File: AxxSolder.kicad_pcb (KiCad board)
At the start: 2 copper layers, 39 x 71 mm, 91 parts, among them IC1 LTC4440AHMS8E-5#PBF, IC2 STM32G431KBT6, IC3 TMP236AQDBZRQ1, IC4 OPA2333AIDRBR, IC5 STM32G431KBT6, IC6 TPS54302DDCR, J1 Conn_01x07_Male, J4 Conn_01x07_Male, Q2 2N7002NXAKR, U1 PEC11L-4220F-S0015, U2 BSC014N04LS

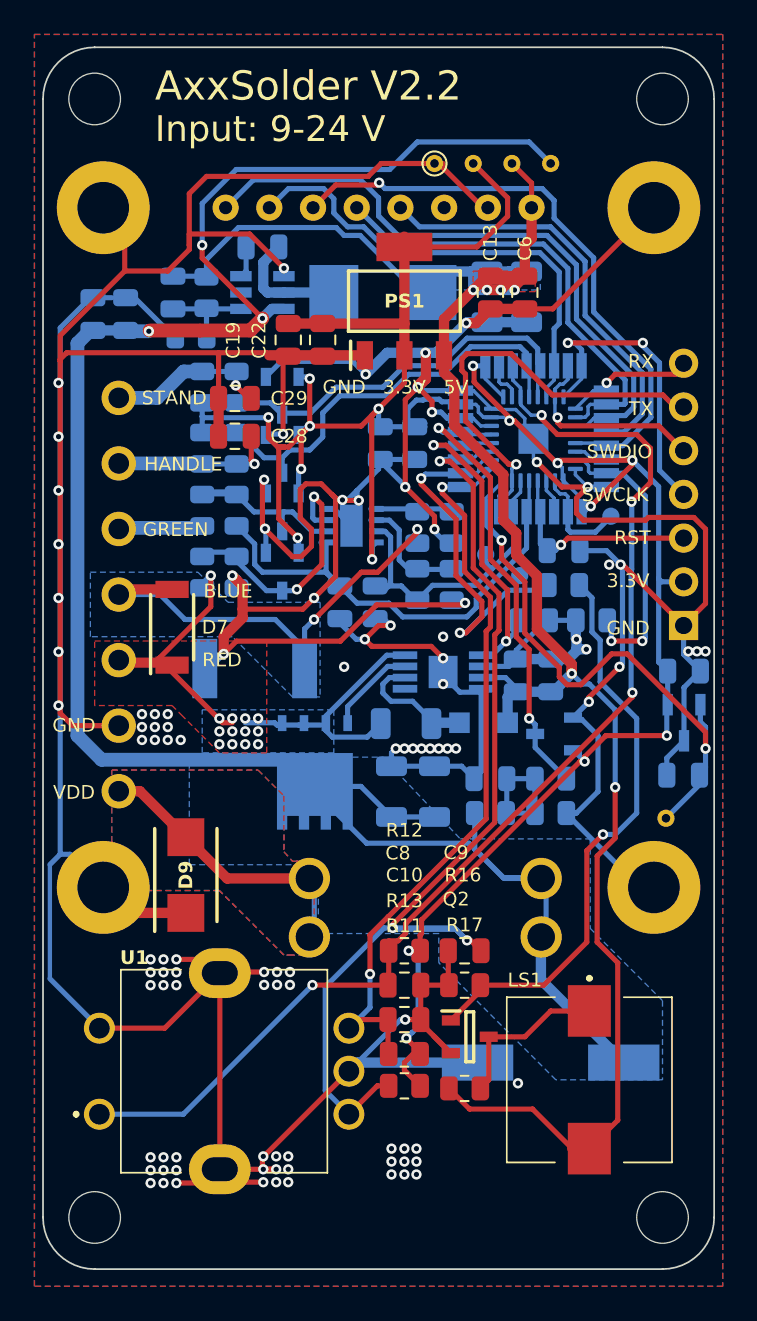
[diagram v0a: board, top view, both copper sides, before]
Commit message: import USB-PD hardware from AxxSolder
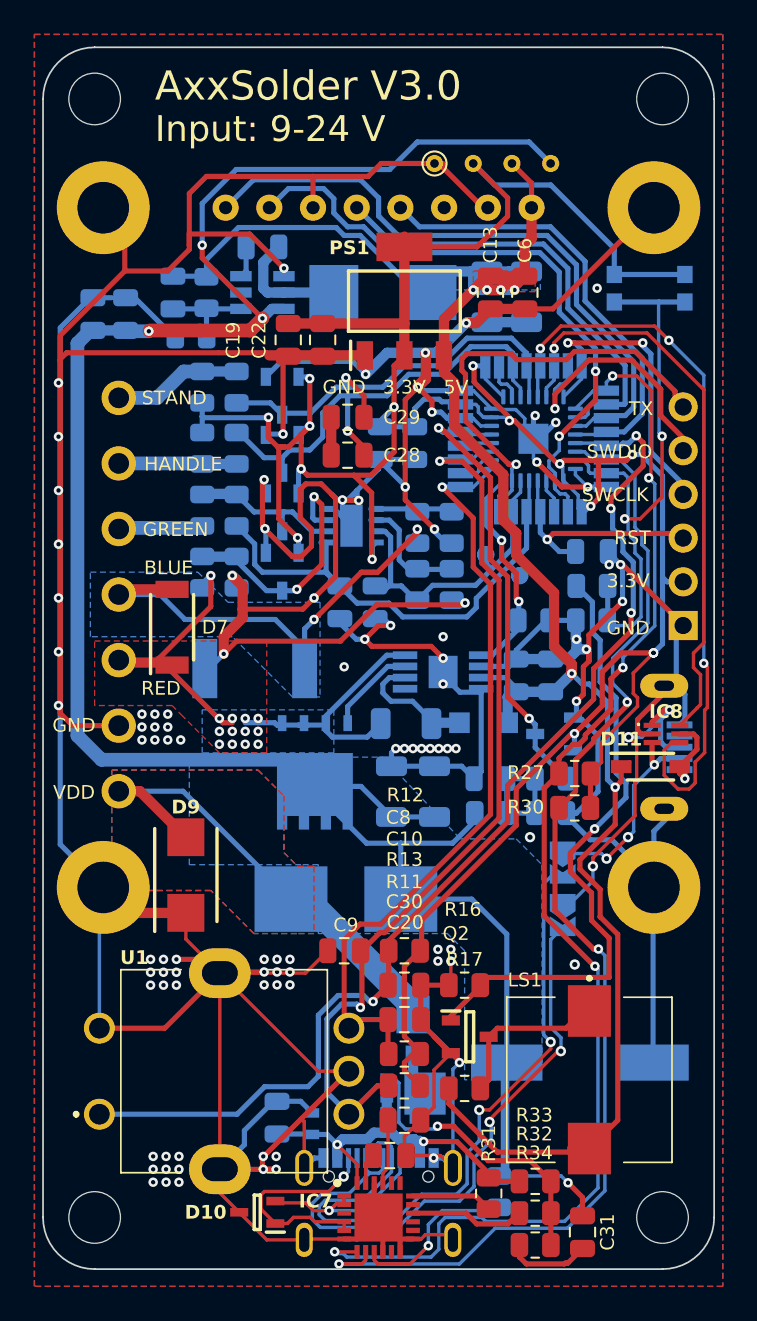
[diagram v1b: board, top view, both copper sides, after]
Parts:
- removed F1: 10A Fuse, 3557-2:3557-2
- removed IC3: TMP236AQDBZRQ1, TMP236AQDBZRQ1:SOT95P237X112-3N
- removed J4: Conn_01x07_Male, Connector_PinSocket_2.54mm:PinSocket_1x07_P2.54mm_Vertical
- removed TP1: AmbTemp_TP, TestPoint:TestPoint_THTPad_D1.0mm_Drill0.5mm
- removed TP2: TestPoint, TestPoint:TestPoint_Pad_D1.0mm
- added C30: 1u, Capacitor_SMD:C_0805_2012Metric, F.Cu at (118.0, 109.3)
- added C31: 100n, Capacitor_SMD:C_0805_2012Metric, F.Cu at (128.3, 115.8)
- added D10: ESDA25W, ESDA25W:SOT65P210X110-3N, F.Cu at (109.5, 114.7)
- added D11: 1N5819HW-7-F, 1N5819HW-7-F:SOD3716X145N, F.Cu at (132.3, 88.8)
- added D13: V7NM103-M3_I, V7NM103-M3_I:V7NM103M3I, B.Cu at (118.5, 103.7)
- added D8: ESDA25P35-1U1M, ESDA25P35-1U1M:ESDA25P351U1M, B.Cu at (112.7, 109.5)
- added F2: 0154007.DRL, 0154007:0154100DR, B.Cu at (114.6, 96.5)
- added IC7: STUSB4500QTR, STUSB4500QTR:QFN50P400X400X100-25N-D, F.Cu at (116.5, 115.0)
- added IC8: USBLC6-2P6, USBLC6-2P6:USBLC62P6, F.Cu at (133.2, 86.9)
- added J2: USB_B_Micro, USB3140-30-0230-1-C_REVE1:GCT_USB3140-30-0230-1-C_REVE1, B.Cu at (132.7, 87.7)
- added J5: USB4105-GF-A-120, USB4105-GF-A:GCT_USB4105-GF-A-120, B.Cu at (116.5, 116.3)
- added J6: Conn_01x06_Socket, Connector_PinSocket_2.54mm:PinSocket_1x06_P2.54mm_Vertical, B.Cu at (134.2, 80.6)
- added JP1: SolderJumper_2_Open, Jumper:SolderJumper-2_P1.3mm_Open_TrianglePad1.0x1.5mm, B.Cu at (127.2, 97.4)
- added JP2: SolderJumper_2_Open, Jumper:SolderJumper-2_P1.3mm_Open_TrianglePad1.0x1.5mm, B.Cu at (127.2, 94.4)
- added Q1: STL9P3LLH6, STL9P3LLH6:STL20N6F7, B.Cu at (118.5, 107.8)
- added R27: 4k7, Resistor_SMD:R_0805_2012Metric, F.Cu at (127.9, 89.2)
- added R30: 4k7, Resistor_SMD:R_0805_2012Metric, F.Cu at (127.9, 91.2)
- added R31: 1k, Resistor_SMD:R_0805_2012Metric, F.Cu at (122.9, 113.6)
- added R32: 22k, Resistor_SMD:R_0805_2012Metric, F.Cu at (125.6, 114.8)
- added R33: 100k, Resistor_SMD:R_0805_2012Metric, F.Cu at (125.6, 112.9)
- added R34: 22k, Resistor_SMD:R_0805_2012Metric, F.Cu at (125.6, 116.6)
- added R35: 1k, Resistor_SMD:R_0805_2012Metric, B.Cu at (123.5, 113.5)
- added S2: KMR211G_LFS, KMR211G_LFS:KMR_2, B.Cu at (132.2, 61.0)
- added TP5: Thermocouple_TP, TestPoint:TestPoint_Pad_D1.0mm, B.Cu at (124.7, 77.7)
- added TP6: Current_TP, TestPoint:TestPoint_Pad_D1.0mm, B.Cu at (122.7, 76.5)
- C20: value 100n -> 1u; moved to F.Cu
- C5: value 100n -> 10u
- moved C5 35.1 mm to (110.6, 109.2), turned to -90 degrees
- moved C20 27.9 mm to (117.2, 111.4), turned to 0 degrees
- moved C9 7.00 mm to (114.5, 99.5)
- moved C28 6.64 mm to (114.7, 70.7)
- moved C29 6.64 mm to (114.7, 68.5)
- moved C23 1.70 mm to (128.2, 106.0), turned to 0 degrees
- moved C7 1.65 mm to (128.9, 76.3)
- moved R15 1.65 mm to (128.9, 78.3), turned to 180 degrees
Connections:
- net /Current renamed /Current_1
- net /MCU_RX renamed /SCL
- net /Thermocouple renamed /Thermocouple_1
- net Net-(IC2-PA8) renamed /HEATER_2
- net Net-(IC2-PB7) renamed /SDA
- net Net-(IC2-PF1-OSC_OUT) renamed /Identification_inp
- net Net-(J1-Pin_7) renamed /VDD_IN
- C20 pad 1: /Ambient_temp -> Net-(IC7-VREG_2V7)
- C28 pad 1: /Handle_sense -> /Handle_inp
- C29 pad 1: /Stand_sense -> /Stand_inp
- C5 pad 1: +3.3V -> GND
- C5 pad 2: GND -> /VBUS
- D4 pad 6: /SPI_CS -> GND
- IC1 pad 1: /Heater -> /Heater_1
- IC2 pad 10: /Buzzer -> /Thermocouple_2
- IC2 pad 12: /Heater -> /Current_2
- IC2 pad 19: /ENC_Button -> /Handle_inp
- IC2 pad 2: Net-(IC2-PF0-OSC_IN) -> /SPI_DC
- IC2 pad 20: /Handle_inp -> /Stand_inp
- IC2 pad 21: /Stand_inp -> /USB_D-
- IC2 pad 22: /SPI_DC -> /USB_D+
- IC2 pad 29: /SPI_CS -> /ENC_Button
- IC2 pad 31: Net-(IC2-PB8-BOOT0) -> /Buzzer
- IC2 pad 8: /Ambient_temp -> /Heater_1
- IC5 pad 10: /Buzzer -> /Thermocouple_2
- IC5 pad 12: /Heater -> /Current_2
- IC5 pad 19: /ENC_Button -> /Handle_inp
- IC5 pad 2: Net-(IC2-PF0-OSC_IN) -> /SPI_DC
- IC5 pad 20: /Handle_inp -> /Stand_inp
- IC5 pad 21: /Stand_inp -> /USB_D-
- IC5 pad 22: /SPI_DC -> /USB_D+
- IC5 pad 29: /SPI_CS -> /ENC_Button
- IC5 pad 31: Net-(IC2-PB8-BOOT0) -> /Buzzer
- IC5 pad 8: /Ambient_temp -> /Heater_1
- R14 pad 2: Net-(IC2-PB8-BOOT0) -> /Buzzer
- R18 pad 1: /Heater -> /Heater_1
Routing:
- net /SCL: track 7.89 -> 76.0 mm, vias 1 -> 5
- net /SDA: track 1.99 -> 69.6 mm, vias 0 -> 3
- net GND: track 451.4 -> 508.9 mm, vias 103 -> 98
- net /USB_D-: track 0.00 -> 43.3 mm, vias 0 -> 3
- net Net-(J5-DN1): track 0.00 -> 39.7 mm, vias 0 -> 2
- net Net-(J5-DP1): track 0.00 -> 35.9 mm, vias 0 -> 2
- net /SPI_CS: track 35.1 -> 0.00 mm, vias 1 -> 0
- net /USB_D+: track 0.00 -> 34.1 mm, vias 0 -> 1
- net /Ambient_temp: track 33.6 -> 0.00 mm, vias 2 -> 0
- net +3.3V: track 153.7 -> 178.0 mm, vias 16 -> 15
- net /VBUS: track 0.00 -> 23.9 mm, vias 0 -> 2
- net /Heater: track 20.4 -> 0.00 mm, vias 2 -> 0
- net /USB_DP: track 0.00 -> 19.9 mm, vias 0 -> 3
- net /USB_PD_GATE: track 0.00 -> 17.2 mm, vias 0 -> 1
- net Net-(IC2-PB8-BOOT0): track 16.7 -> 0.00 mm, vias 2 -> 0
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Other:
- board text added: "3.3"
- board text added: "AxxSolder V3.0"
- board text added: "BOOT"
- board text added: "USBC_DN"
- board text added: "USBC_DP"
- board text removed: "AxxSolder V2.2"
- board text removed: "RX"
- board text removed: "TMP"
